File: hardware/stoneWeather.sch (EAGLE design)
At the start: 27 parts, among them IC1 ATMEGA328, IC2 AMS1117

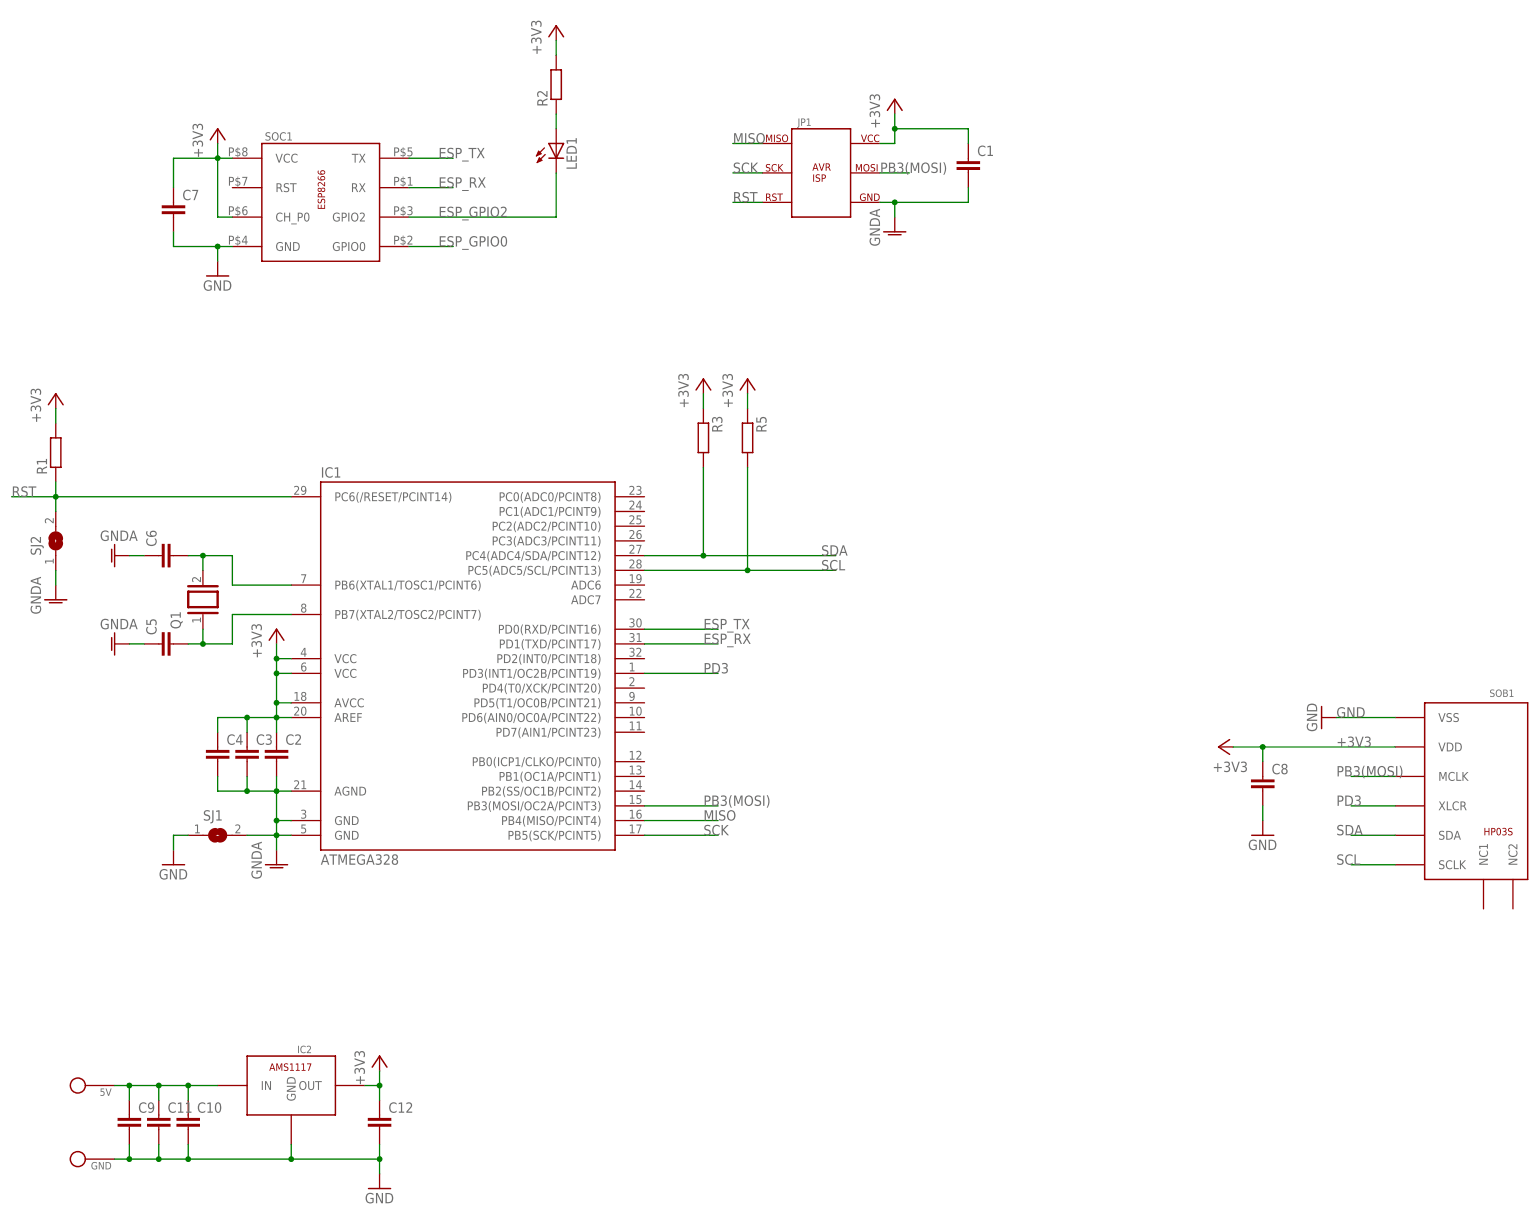
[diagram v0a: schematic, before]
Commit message: Added GY21-HTU21 breakout board header to the board Updated README.md
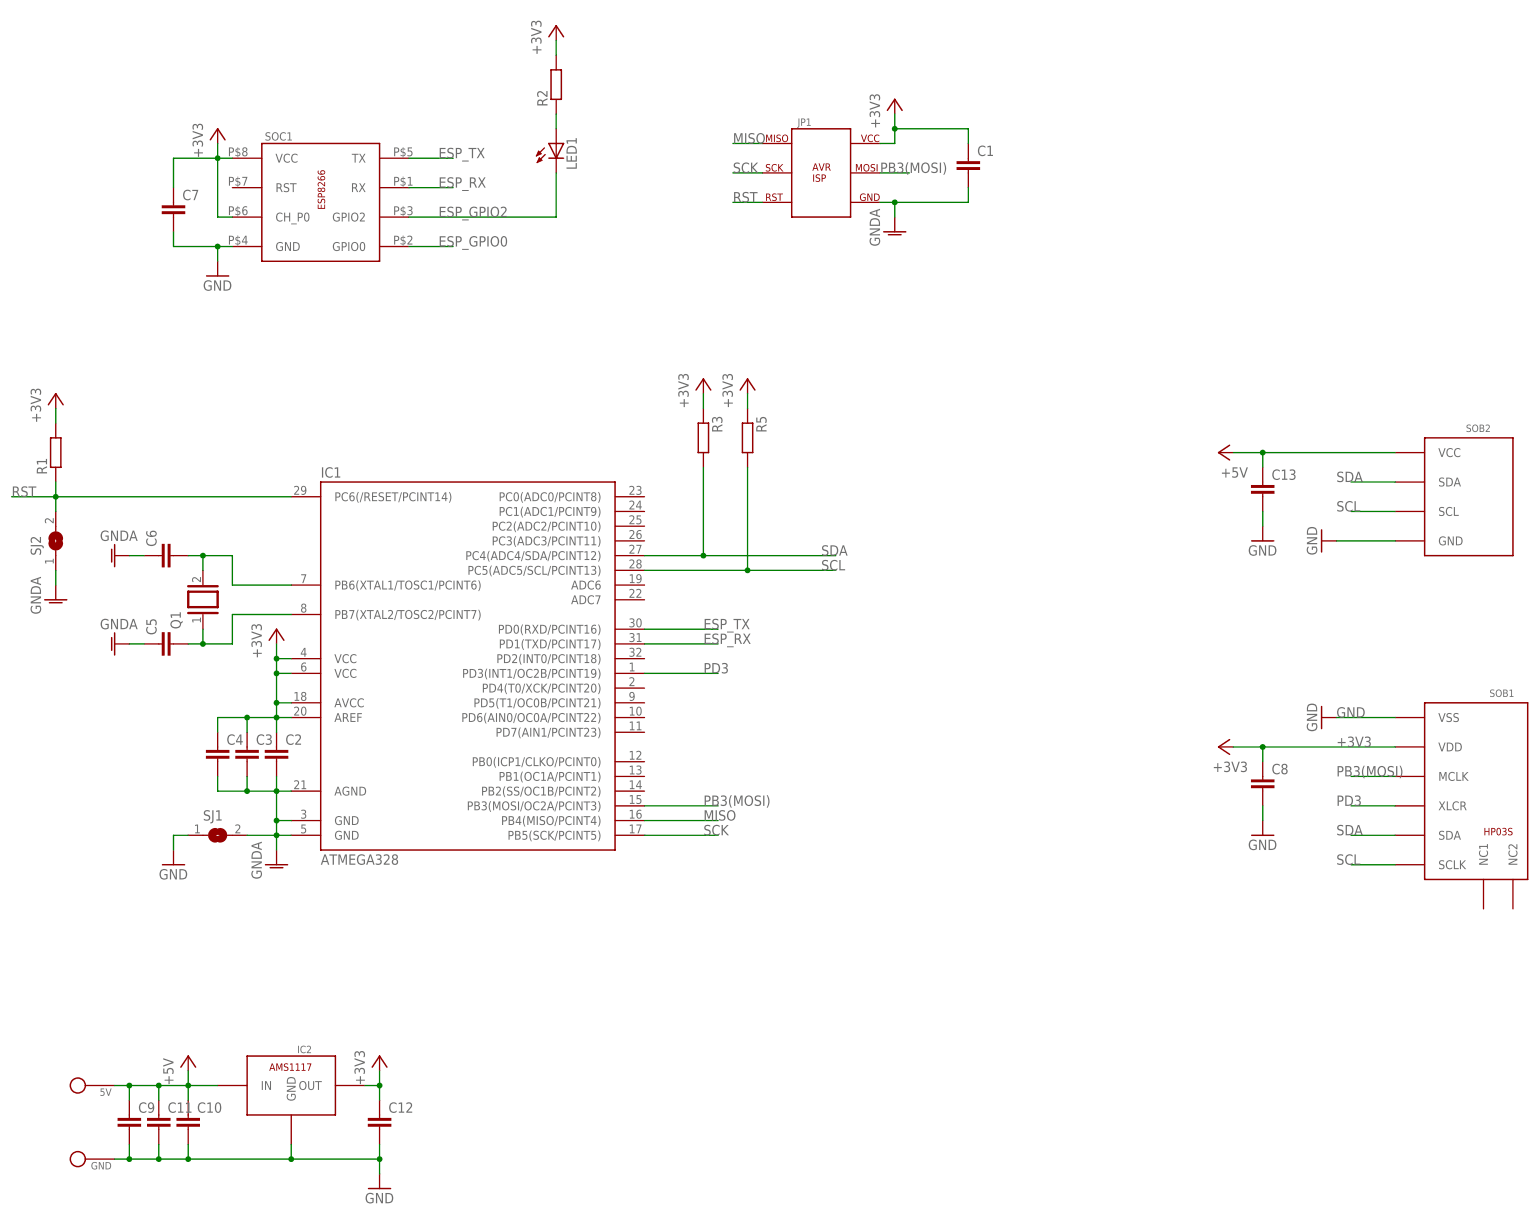
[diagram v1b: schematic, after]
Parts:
- added C13: (no value), rcl:C-EUC0805
- added SOB2: (no value), stoneTronics:GY21_HTU21
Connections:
- removed net N$2: 5V.P$1, C10.1, C11.1, C9.1, IC2.IN
- new net +5V: 5V.P$1, C10.1, C11.1, C13.1, C9.1, IC2.IN, SOB2.VCC
- net GND: now also C13.2, SOB2.GND
- net SCL: now also SOB2.SCL
- net SDA: now also SOB2.SDA
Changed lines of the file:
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@@
 <part name="GND10" library="supply1" deviceset="GND" device=""/>
 <part name="+3V9" library="supply1" deviceset="+3V3" device=""/>
+<part name="SOB2" library="stoneTronics" deviceset="GY21_HTU21" device=""/>
+<part name="P+1" library="supply1" deviceset="+5V" device=""/>
+<part name="P+2" library="supply1" deviceset="+5V" device=""/>
+<part name="GND11" library="supply1" deviceset="GND" device=""/>
+<part name="C13" library="rcl" deviceset="C-EU" device="C0805"/>
+<part name="GND12" library="supply1" deviceset="GND" device=""/>
 </parts>
 <sheets>
@@
 <instance part="GND10" gate="1" x="91.44" y="43.18"/>
 <instance part="+3V9" gate="G$1" x="91.44" y="66.04"/>
+<instance part="SOB2" gate="G$1" x="279.4" y="162.56"/>
+<instance part="P+1" gate="1" x="58.42" y="66.04"/>
+<instance part="P+2" gate="1" x="236.22" y="170.18" rot="R90"/>
+<instance part="GND11" gate="1" x="254" y="154.94" rot="R270"/>
+<instance part="C13" gate="G$1" x="243.84" y="165.1"/>
+<instance part="GND12" gate="1" x="243.84" y="154.94"/>
 </instances>
 <busses>
@@
 <junction x="91.44" y="48.26"/>
 <pinref part="GND10" gate="1" pin="GND"/>
+</segment>
+<segment>
+<pinref part="SOB2" gate="G$1" pin="GND"/>
+<pinref part="GND11" gate="1" pin="GND"/>
+<wire x1="256.54" y1="154.94" x2="266.7" y2="154.94" width="0.1524" layer="91"/>
+</segment>
+<segment>
+<pinref part="C13" gate="G$1" pin="2"/>
+<pinref part="GND12" gate="1" pin="GND"/>
+<wire x1="243.84" y1="157.48" x2="243.84" y2="160.02" width="0.1524" layer="91"/>
 </segment>
 </net>
@@
 <label x="256.54" y="104.14" size="1.778" layer="95"/>
 </segment>
+<segment>
+<pinref part="SOB2" gate="G$1" pin="SDA"/>
+<wire x1="266.7" y1="165.1" x2="259.08" y2="165.1" width="0.1524" layer="91"/>
+<label x="256.54" y="165.1" size="1.778" layer="95"/>
+</segment>
 </net>
 <net name="SCL" class="0">
@@
 <label x="256.54" y="99.06" size="1.778" layer="95"/>
 </segment>
+<segment>
+<pinref part="SOB2" gate="G$1" pin="SCL"/>
+<wire x1="266.7" y1="160.02" x2="259.08" y2="160.02" width="0.1524" layer="91"/>
+<label x="256.54" y="160.02" size="1.778" layer="95"/>
+</segment>
 </net>
 <net name="PD3" class="0">
@@
 </segment>
 </net>
-<net name="N$2" class="0">
+<net name="+5V" class="0">
 <segment>
 <pinref part="5V" gate="G$1" pin="P$1"/>
@@
 <junction x="53.34" y="60.96"/>
 <junction x="58.42" y="60.96"/>
-</segment>
-</net>
+<pinref part="P+1" gate="1" pin="+5V"/>
+<wire x1="58.42" y1="60.96" x2="58.42" y2="63.5" width="0.1524" layer="91"/>
+</segment>
+<segment>
+<pinref part="SOB2" gate="G$1" pin="VCC"/>
+<pinref part="P+2" gate="1" pin="+5V"/>
+<wire x1="238.76" y1="170.18" x2="243.84" y2="170.18" width="0.1524" layer="91"/>
+<pinref part="C13" gate="G$1" pin="1"/>
+<wire x1="243.84" y1="170.18" x2="266.7" y2="170.18" width="0.1524" layer="91"/>
+<wire x1="243.84" y1="167.64" x2="243.84" y2="170.18" width="0.1524" layer="91"/>
+<junction x="243.84" y="170.18"/>
+</segment>
+</net>
